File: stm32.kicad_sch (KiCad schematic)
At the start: 22 parts, among them IC1 ADBMS6821CCSZ, J5 Conn_02x03_Top_Bottom, SW3 SW_Nidec_CAS-120A1, T1 74941301, U15 SN65HVD235, U3 STM32G474CETx, Y2 16 MHz

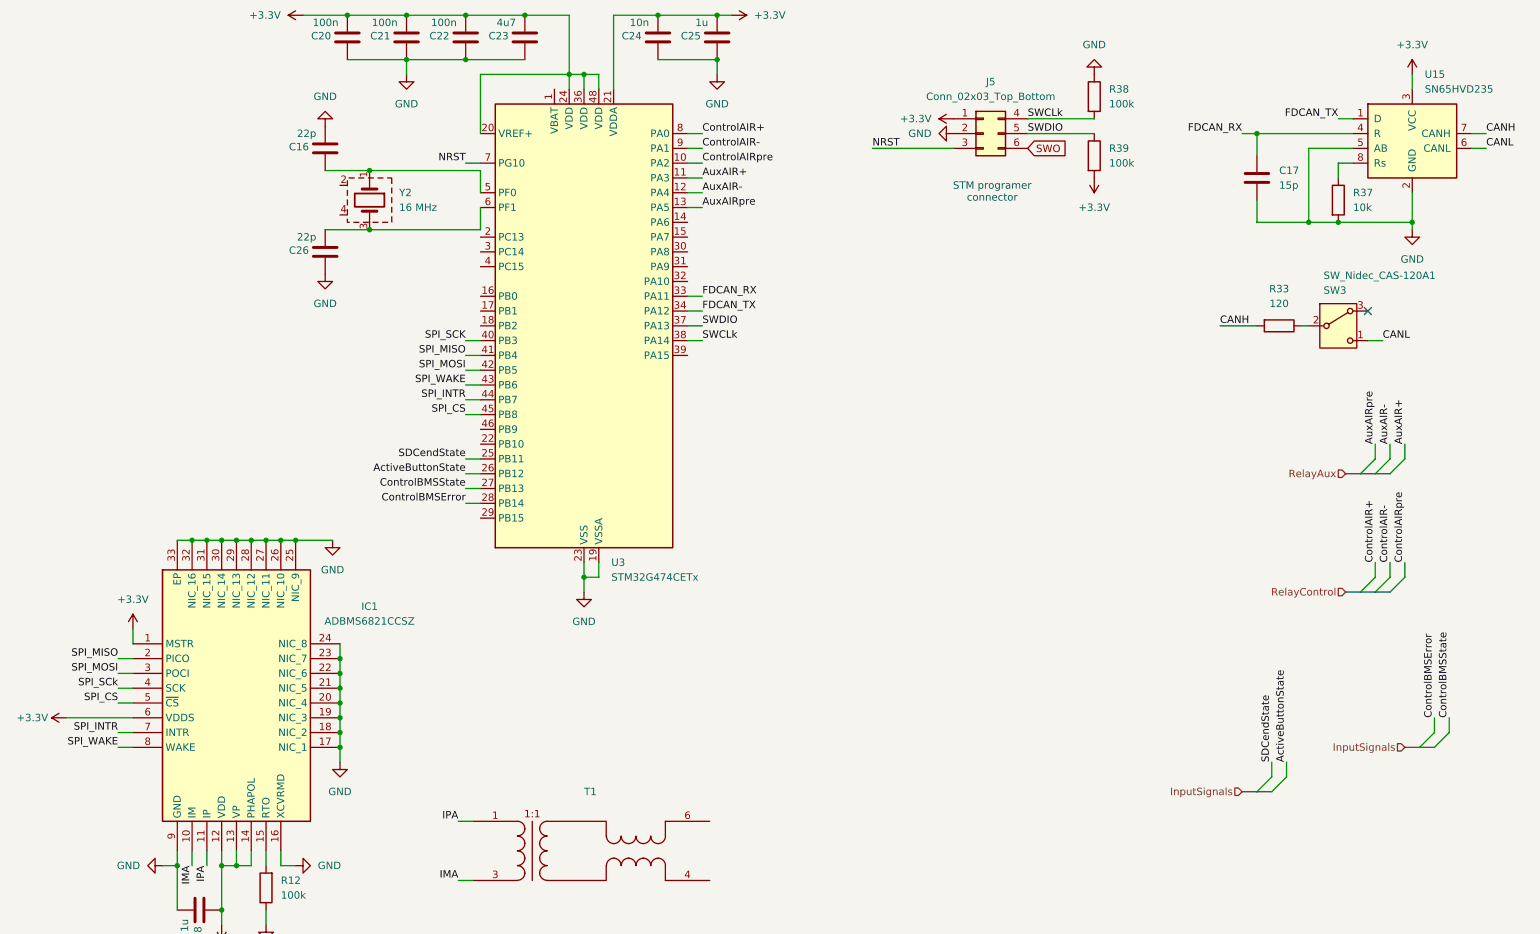
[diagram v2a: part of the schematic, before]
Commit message: - Reubicació dels inputs/outputs del STM32 - Ampliació a un segon can FDCAN2 amb un segon tranceptor
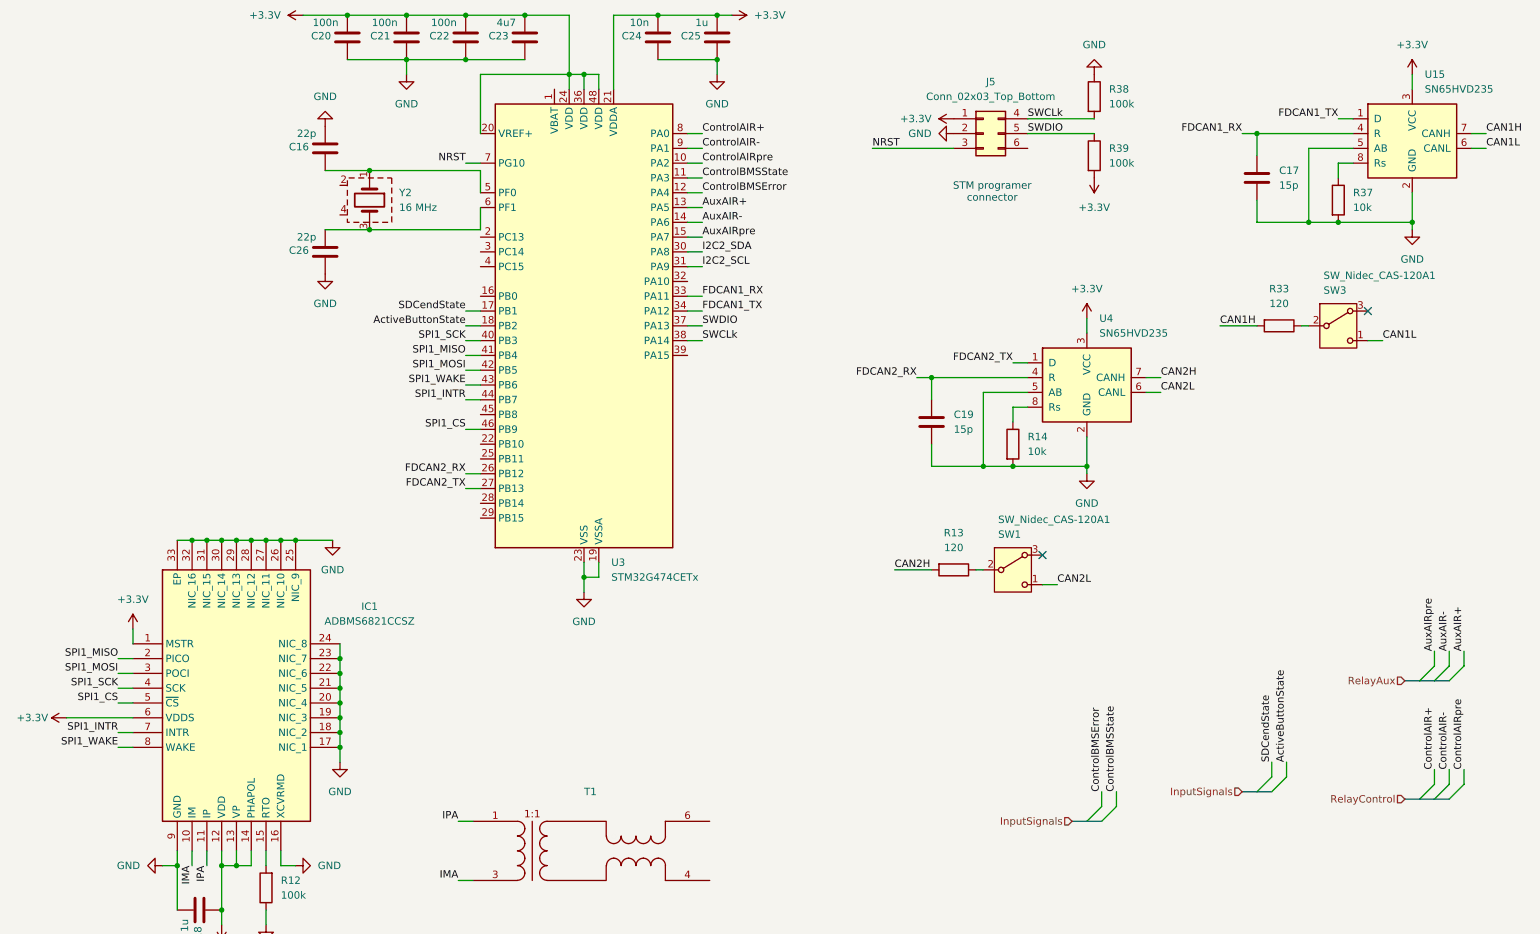
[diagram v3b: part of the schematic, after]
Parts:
- added C19: 15p, Capacitor_SMD:C_0603_1608Metric_Pad1.08x0.95mm_HandSolder, symbol Device:C
- added R13: 120, Resistor_SMD:R_0201_0603Metric_Pad0.64x0.40mm_HandSolder, symbol Device:R
- added R14: 10k, Resistor_SMD:R_0201_0603Metric_Pad0.64x0.40mm_HandSolder, symbol Device:R
- added SW1: SW_Nidec_CAS-120A1, Button_Switch_SMD:Nidec_Copal_CAS-120A, symbol Switch:SW_Nidec_CAS-120A1
- added U4: SN65HVD235, Package_SO:SOIC-8_3.9x4.9mm_P1.27mm, symbol Interface_CAN_LIN:SN65HVD235
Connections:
- net SPI_SCk is gone; now on net SPI1_SCK: IC1.4 (SCK)
- net +3.3V: now also U4.3 (VCC)
- net ActiveButtonState: now also U3.18 (PB2); no longer U3.26 (PB12)
- net AuxAIR+: now also U3.13 (PA5); no longer U3.11 (PA3)
- net AuxAIR-: now also U3.14 (PA6); no longer U3.12 (PA4)
- net AuxAIRpre: now also U3.15 (PA7); no longer U3.13 (PA5)
- net ControlBMSError: now also U3.12 (PA4); no longer U3.28 (PB14)
- net ControlBMSState: now also U3.11 (PA3); no longer U3.27 (PB13)
- net GND: now also C19.2, R14.2, U4.2 (GND), U4.5 (AB)
- net SDCendState: now also U3.17 (PB1); no longer U3.25 (PB11)
- net I2C2_SDA: now reaches U3.30 (PA8)
- net I2C2_SCL: now reaches U3.31 (PA9)
- net SPI1_CS: now reaches U3.46 (PB9)
- net SPI1_CS: now also IC1.5 (~{CS})
- net CANH renamed CAN1H
- net CANL renamed CAN1L
- net FDCAN_RX renamed FDCAN1_RX
- net FDCAN_TX renamed FDCAN1_TX
- net SPI_CS: no longer names the net of U3.45 (PB8)
- net SPI_CS: no longer IC1.5 (~{CS})
- net SPI_INTR renamed SPI1_INTR
- net SPI_MISO renamed SPI1_MISO
- net SPI_MOSI renamed SPI1_MOSI
- net SPI_SCK renamed SPI1_SCK
- net SPI_WAKE renamed SPI1_WAKE
- net SWO: no longer names the net of J5.6 (Pin_6)
- new net: R14.1, U4.8 (Rs)
- new net: R13.1, SW1.2 (B)
- new net CAN2H: R13.2, U4.7 (CANH)
- new net CAN2L: SW1.1 (C), U4.6 (CANL)
- new net FDCAN2_RX: C19.1, U3.26 (PB12), U4.4 (R)
- new net FDCAN2_TX: U3.27 (PB13), U4.1 (D)
- no-connect marks 1 -> 2

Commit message: - Reorganització dels components al fitxer de stm32 - S'ha afegit el ADC ADS1113IDGS per la lectura del sensor Hall - Modificació del tranceptor CAN al SN65HVD234 - Eliminació del pin SWO - S'ha afegit el pin de enable per a cada tranceptor
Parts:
- removed R38, R39: 100k, Resistor_SMD:R_0201_0603Metric_Pad0.64x0.40mm_HandSolder, symbol Device:R
- added C10, C11, C9: 100n, Capacitor_SMD:C_0603_1608Metric_Pad1.08x0.95mm_HandSolder, symbol Device:C
- added R17, R18: 100k, Resistor_SMD:R_0201_0603Metric_Pad0.64x0.40mm_HandSolder, symbol Device:R
- added U5: ADS1113IDGS, Package_SO:TSSOP-10_3x3mm_P0.5mm, symbol Analog_ADC:ADS1113IDGS
- U15, U4: value SN65HVD235 -> SN65HVD234; symbol Interface_CAN_LIN:SN65HVD235 -> Interface_CAN_LIN:SN65HVD234
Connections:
- net +3.3V: now also C10.1, C11.1, C9.1, R17.1, U5.8 (VDD)
- net GND: now also C10.2, C11.2, C9.2, R18.2, U5.1 (ADDR), U5.3 (GND); no longer U15.5 (AB), U4.5 (AB)
- net I2C2_SCL: now also U5.10 (SCL)
- net I2C2_SDA: now also U5.9 (SDA)
- net SWDIO: now also R17.2
- net FDCAN1_EN: now reaches U3.2 (PC13)
- net FDCAN1_EN: now also U15.5 (EN)
- net FDCAN2_EN: now reaches U3.3 (PC14)
- net FDCAN2_EN: now also U4.5 (EN)
- net IMA_EXT: now reaches T1.4
- net IPA_EXT: now reaches T1.6
- net SWCLk renamed SWCLK
- net SWCLK: now also R18.1
- new net HallVout: U5.4 (AIN0)
- no-connect marks 2 -> 13
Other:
- note added: "CANBUS SYSTEM"
- note added: "EXTERNAL ADC (I2C)"
- note added: "MICROCONTROLLER PINOUT ASSIGNMENT"
- note added: "SPI TO ISOSPI TRANSCEIVER"
- note added: "STM32 PROGRAMMING CONNECTOR"
- note removed: "STM programer connector"
- moved on the sheet: C16, C17, C18, C19, C20, C21, C22, C23, C24, C25, C26, IC1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

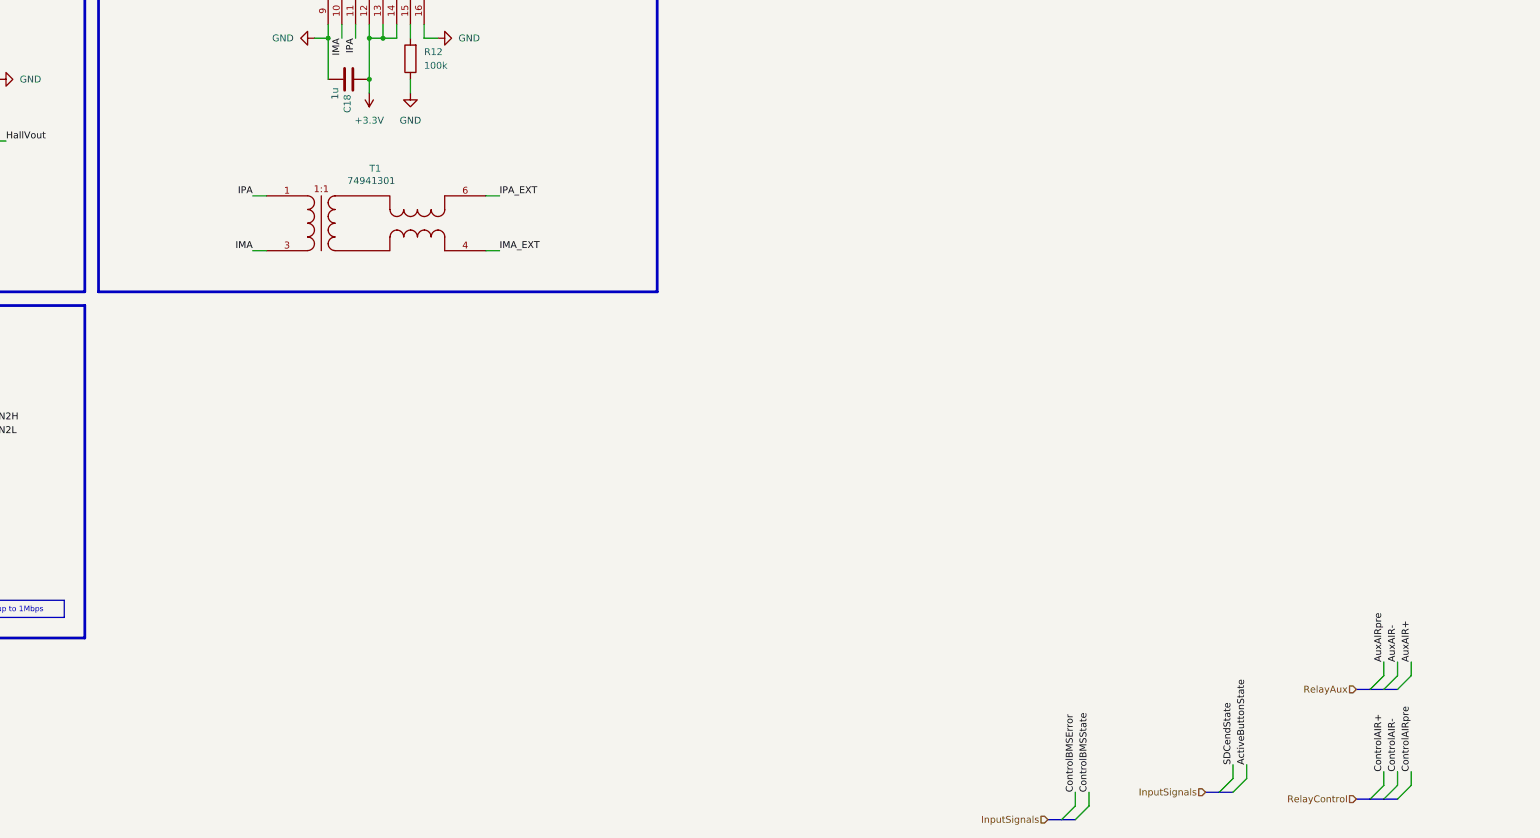
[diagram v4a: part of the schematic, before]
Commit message: S'ha afegit llista to do amb els canvis a fer i s'ha girat el circuit de l'entrada d'auxiliars per millor comprensió
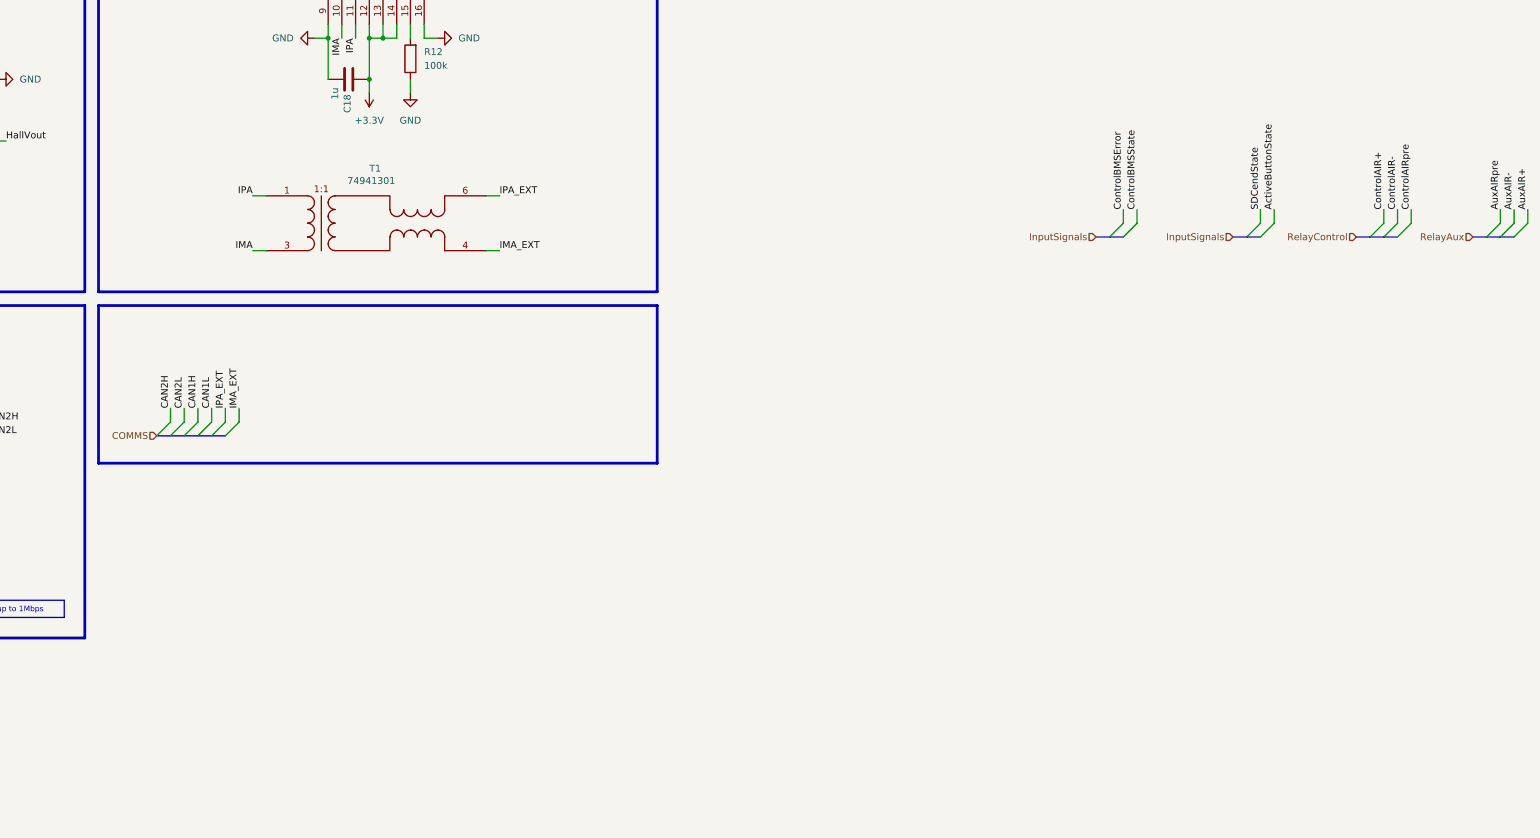
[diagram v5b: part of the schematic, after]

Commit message: - S'han afegit uns connectors preliminar \n-S'han eliminat els diodes de protecció dels airs
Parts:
- added R19, R20: 100k, Resistor_SMD:R_0201_0603Metric_Pad0.64x0.40mm_HandSolder, symbol Device:R
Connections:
- net GND: now also R20.1
- net ControlBMSError: no longer names the net of U3.12 (PA4)
- net ControlBMSState: no longer names the net of U3.11 (PA3)
- new net +5V: R19.2
- new net HallVref: R19.1, R20.2
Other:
- moved on the sheet: C11, U5

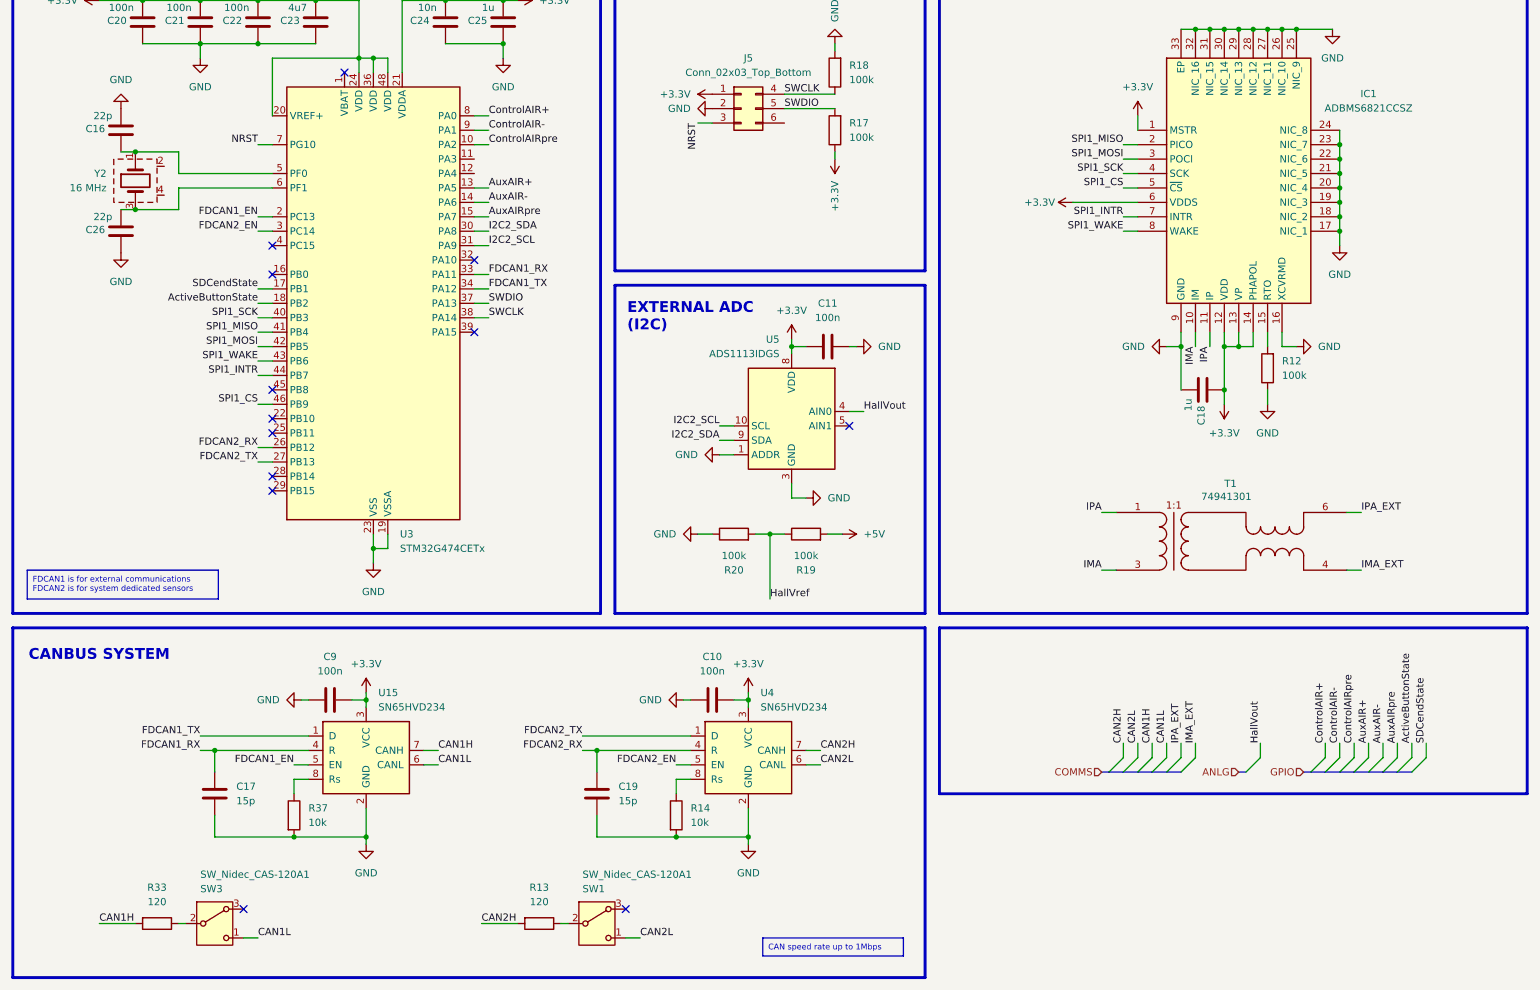
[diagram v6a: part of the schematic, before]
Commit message: Modificació de les etiquetes a globals Filtre afegit al transformador de isoSPI Leds indicadors per estat i error Senyal d'error de BMS per el sdcreset
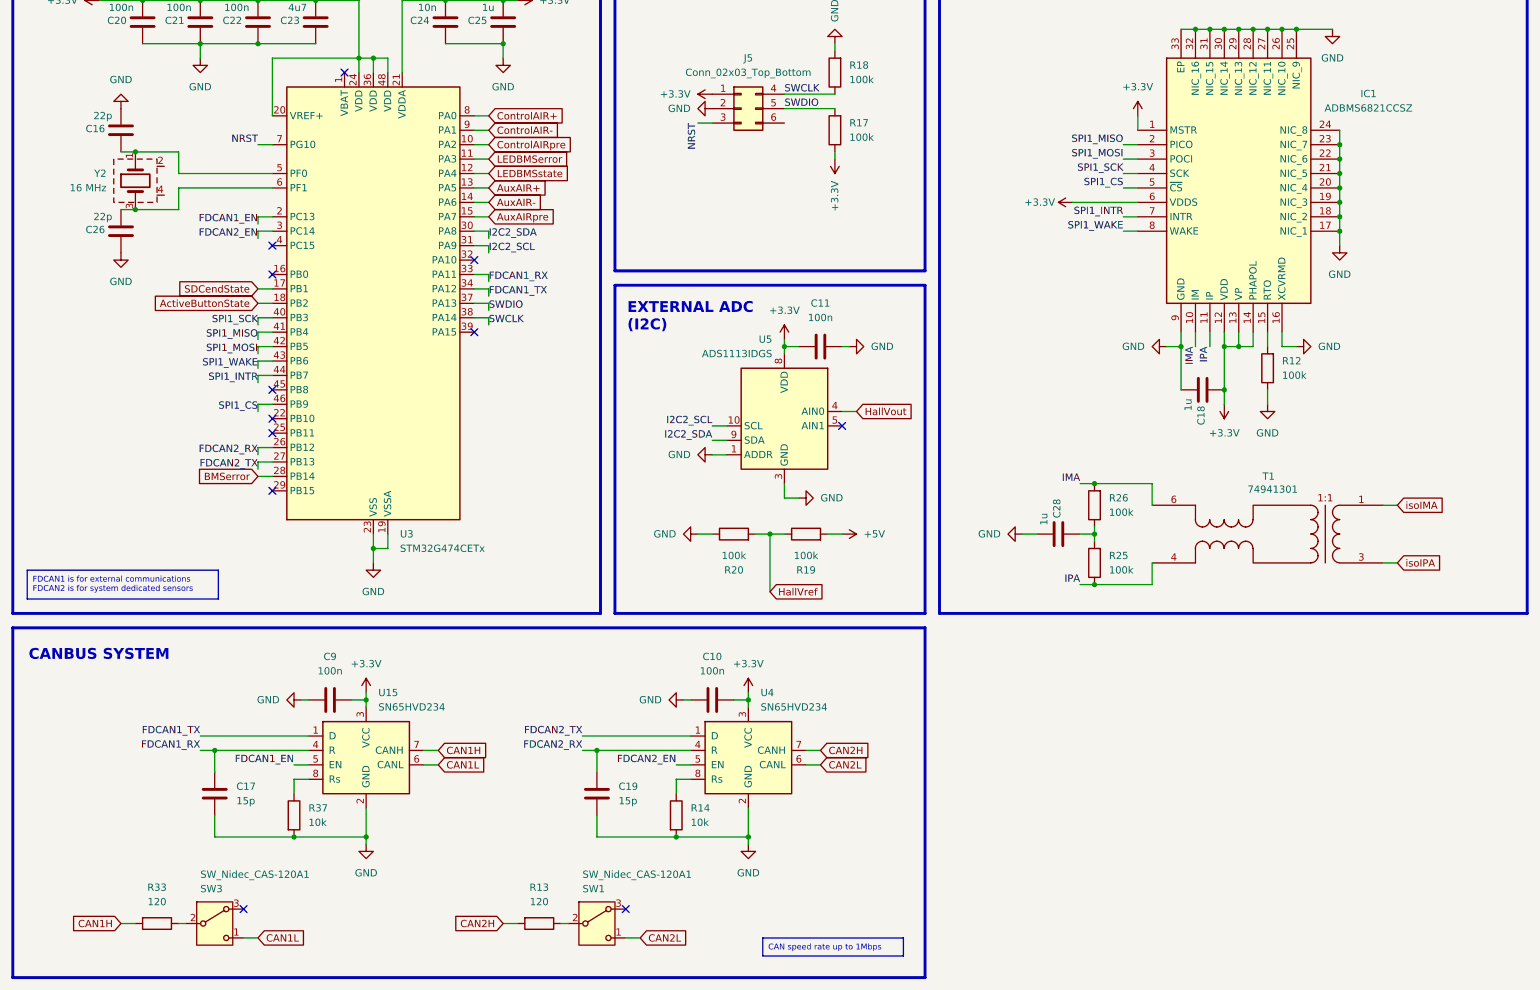
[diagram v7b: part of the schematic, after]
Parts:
- added C28: 1u, Capacitor_SMD:C_0603_1608Metric_Pad1.08x0.95mm_HandSolder, symbol Device:C
- added R25, R26: 100k, Resistor_SMD:R_0201_0603Metric_Pad0.64x0.40mm_HandSolder, symbol Device:R
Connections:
- net IMA_EXT is gone; now on net IPA: T1.4
- net IPA_EXT is gone; now on net IMA: T1.6
- net GND: now also C28.2
- net IMA: now also R26.2; no longer T1.3
- net IPA: now also R25.1; no longer T1.1
- net LEDBMSerror: now reaches U3.11 (PA3)
- net LEDBMSstate: now reaches U3.12 (PA4)
- net BMSerror: now reaches U3.28 (PB14)
- new net: C28.1, R25.2, R26.1
- new net isoIMA: T1.1
- new net isoIPA: T1.3
- no-connect marks 13 -> 12
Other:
- moved on the sheet: C11, T1, U5
